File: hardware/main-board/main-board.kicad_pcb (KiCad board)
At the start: 4 copper layers, 105 x 38 mm, 105 parts, among them J1 USB_C_Receptacle_USB2.0, J2 DNI, J3 Display Connector, J4 Conn_01x04, SW1 SW_Push, SW2 SW_Push, SW3 SW_Push, SW4 SW_Push, SW5 SW_Detect, SW6 SW_Boot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

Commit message: Final tweaks for Rev C manufacture
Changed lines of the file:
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@@
 	(title_block
 		(title "Printalyzer UV/VIS Densitometer - Main Board")
-		(date "2024-09-04")
+		(date "2024-09-24")
 		(rev "C")
 		(company "Dektronics, Inc.")
@@
 			(pinfunction "Pin_2")
 			(pintype "passive")
+			(teardrops
+				(best_length_ratio 0.5)
+				(max_length 1)
+				(best_width_ratio 1)
+				(max_width 2)
+				(curve_points 0)
+				(filter_ratio 0.9)
+				(enabled yes)
+				(allow_two_segments yes)
+				(prefer_zone_connections yes)
+			)
 		)
 		(pad "3" smd roundrect
@@
 			(pinfunction "Pin_3")
 			(pintype "passive")
+			(teardrops
+				(best_length_ratio 0.5)
+				(max_length 1)
+				(best_width_ratio 1)
+				(max_width 2)
+				(curve_points 0)
+				(filter_ratio 0.9)
+				(enabled yes)
+				(allow_two_segments yes)
+				(prefer_zone_connections yes)
+			)
 		)
 		(pad "4" smd roundrect
@@
 		(start 61.3 61.066002)
 		(end 61.13 61.236002)
-		(width 0.254)
+		(width 0.2)
 		(layer "F.Cu")
 		(net 1)
@@
 		(start 62.213 55.636)
 		(end 62.336 55.759)
-		(width 0.254)
+		(width 0.2)
 		(layer "F.Cu")
 		(net 1)
@@
 		(start 61.13 61.236002)
 		(end 61.13 61.65)
-		(width 0.254)
+		(width 0.2)
 		(layer "F.Cu")
 		(net 1)
@@
 		(start 62.336 57.537)
 		(end 62.463 57.664)
-		(width 0.254)
+		(width 0.2)
 		(layer "F.Cu")
 		(net 1)
@@
 		(start 61.5 56.636)
 		(end 62.324 56.636)
-		(width 0.254)
+		(width 0.2)
 		(layer "F.Cu")
 		(net 1)
@@
 		(start 61.3 60.2625)
 		(end 61.3 61.066002)
-		(width 0.254)
+		(width 0.2)
 		(layer "F.Cu")
 		(net 1)
@@
 		(start 62.336 56.648)
 		(end 62.336 57.537)
-		(width 0.254)
+		(width 0.2)
 		(layer "F.Cu")
 		(net 1)
@@
 		(start 61.5 55.636)
 		(end 62.213 55.636)
-		(width 0.254)
+		(width 0.2)
 		(layer "F.Cu")
 		(net 1)
@@
 		(start 62.463 57.664)
 		(end 62.971 57.664)
-		(width 0.254)
+		(width 0.2)
 		(layer "F.Cu")
 		(net 1)
@@
 		(start 61.5 56.136)
 		(end 62.332 56.136)
-		(width 0.254)
+		(width 0.2)
 		(layer "F.Cu")
 		(net 1)
@@
 		(start 62.336 56.14)
 		(end 62.336 56.648)
-		(width 0.254)
+		(width 0.2)
 		(layer "F.Cu")
 		(net 1)
@@
 		(start 62.336 55.759)
 		(end 62.336 56.14)
-		(width 0.254)
+		(width 0.2)
 		(layer "F.Cu")
 		(net 1)
@@
 		(start 62.971 56.874)
 		(end 62.971 57.664)
-		(width 0.508)
+		(width 0.381)
 		(layer "F.Cu")
 		(net 1)
@@
 		(start 63.761 55.914)
 		(end 63.86 56.013)
-		(width 0.508)
+		(width 0.381)
 		(layer "F.Cu")
 		(net 2)
@@
 		(start 62.971 55.378)
 		(end 62.971 55.914)
-		(width 0.254)
+		(width 0.2)
 		(layer "F.Cu")
 		(net 2)
@@
 		(start 62.971 55.914)
 		(end 63.761 55.914)
-		(width 0.508)
+		(width 0.381)
 		(layer "F.Cu")
 		(net 2)
@@
 		(start 61.5 55.136)
 		(end 62.729 55.136)
-		(width 0.254)
+		(width 0.2)
 		(layer "F.Cu")
 		(net 2)
@@
 		(start 62.729 55.136)
 		(end 62.971 55.378)
-		(width 0.254)
+		(width 0.2)
 		(layer "F.Cu")
 		(net 2)
@@
 		(start 60 60.2625)
 		(end 60 61.066002)
-		(width 0.254)
+		(width 0.2)
 		(layer "F.Cu")
 		(net 7)
@@
 		(start 60 61.066002)
 		(end 60.17 61.236002)
-		(width 0.254)
+		(width 0.2)
 		(layer "F.Cu")
 		(net 7)
@@
 		(start 60.17 61.236002)
 		(end 60.17 61.65)
-		(width 0.254)
+		(width 0.2)
 		(layer "F.Cu")
 		(net 7)
@@
 		(start 60 59.7375)
 		(end 60 59.4428)
-		(width 0.254)
+		(width 0.2)
 		(layer "F.Cu")
 		(net 23)
@@
 		(start 60 59.4428)
 		(end 59.542 58.9848)
-		(width 0.254)
+		(width 0.2)
 		(layer "F.Cu")
 		(net 23)
@@
 		(start 56.506 55.136)
 		(end 55.986 54.616)
-		(width 0.254)
+		(width 0.2)
 		(layer "F.Cu")
 		(net 23)
@@
 		(start 56.6718 58.9848)
 		(end 56.494 58.807)
-		(width 0.254)
+		(width 0.2)
 		(layer "F.Cu")
 		(net 23)
@@
 		(start 58.6 55.136)
 		(end 56.506 55.136)
-		(width 0.254)
+		(width 0.2)
 		(layer "F.Cu")
 		(net 23)
@@
 		(start 59.542 58.9848)
 		(end 56.6718 58.9848)
-		(width 0.254)
+		(width 0.2)
 		(layer "F.Cu")
 		(net 23)
@@
 		(start 61.3 58.533)
 		(end 61.3 59.7375)
-		(width 0.254)
+		(width 0.2)
 		(layer "F.Cu")
 		(net 24)
@@
 		(start 58.6 55.636)
 		(end 55.863 55.636)
-		(width 0.254)
+		(width 0.2)
 		(layer "F.Cu")
 		(net 24)
@@
 		(start 55.351 58.1466)
 		(end 55.3574 58.153)
-		(width 0.254)
+		(width 0.2)
 		(layer "F.Cu")
 		(net 24)
@@
 		(start 55.3574 58.153)
 		(end 60.92 58.153)
-		(width 0.254)
+		(width 0.2)
 		(layer "F.Cu")
 		(net 24)
@@
 		(start 60.92 58.153)
 		(end 61.3 58.533)
-		(width 0.254)
+		(width 0.2)
 		(layer "F.Cu")
 		(net 24)
@@
 		(start 55.863 55.636)
 		(end 54.843 54.616)
-		(width 0.254)
+		(width 0.2)
 		(layer "F.Cu")
 		(net 24)
@@
 		(start 60.65 59.7375)
 		(end 60.65 59.1)
-		(width 0.254)
+		(width 0.2)
 		(layer "F.Cu")
 		(net 57)
@@
 		(start 60.65 60.2625)
 		(end 60.65 60.9)
-		(width 0.254)
+		(width 0.2)
 		(layer "F.Cu")
 		(net 61)
@@
 		(priority 6)
 		(connect_pads yes
-			(clearance 0.508)
+			(clearance 0.25)
 		)
 		(min_thickness 0.25)
@@
 		(priority 7)
 		(connect_pads yes
-			(clearance 0.508)
+			(clearance 0.25)
 		)
 		(min_thickness 0.25)
@@
 		(priority 6)
 		(connect_pads yes
-			(clearance 0.508)
+			(clearance 0.25)
 		)
 		(min_thickness 0.25)
@@
 		(priority 7)
 		(connect_pads yes
-			(clearance 0.508)
+			(clearance 0.25)
 		)
 		(min_thickness 0.25)
@@
 		(priority 7)
 		(connect_pads yes
-			(clearance 0.508)
+			(clearance 0.25)
 		)
 		(min_thickness 0.25)
@@
 		(priority 6)
 		(connect_pads yes
-			(clearance 0.508)
+			(clearance 0.25)
 		)
 		(min_thickness 0.25)
@@
 		(priority 7)
 		(connect_pads yes
-			(clearance 0.508)
+			(clearance 0.25)
 		)
 		(min_thickness 0.25)
@@
 	)
 	(zone
+		(net 58)
+		(net_name "/TVLED_EN")
+		(layer "F.Cu")
+		(name "$teardrop_padvia$")
+		(hatch full 0.1)
+		(priority 30000)
+		(attr
+			(teardrop
+				(type padvia)
+			)
+		)
+		(connect_pads yes
+			(clearance 0)
+		)
+		(min_thickness 0.0254)
+		(filled_areas_thickness no)
+		(fill yes
+			(thermal_gap 0.5)
+			(thermal_bridge_width 0.5)
+			(island_removal_mode 1)
+			(island_area_min 10)
+		)
+		(polygon
+			(pts
+				(xy 140.599993 70.373012) (xy 140.599993 70.627012) (xy 140.99259 70.788594) (xy 141.675993 70.500012)
+				(xy 140.99259 70.21143)
+			)
+		)
+	)
+	(zone
+		(net 60)
+		(net_name "/TULED_EN")
+		(layer "F.Cu")
+		(name "$teardrop_padvia$")
+		(hatch full 0.1)
+		(priority 30001)
+		(attr
+			(teardrop
+				(type padvia)
+			)
+		)
+		(connect_pads yes
+			(clearance 0)
+		)
+		(min_thickness 0.0254)
+		(filled_areas_thickness no)
+		(fill yes
+			(thermal_gap 0.5)
+			(thermal_bridge_width 0.5)
+			(island_removal_mode 1)
+			(island_area_min 10)
+		)
+		(polygon
+			(pts
+				(xy 140.599993 69.373012) (xy 140.599993 69.627012) (xy 140.99259 69.788594) (xy 141.675993 69.500012)
+				(xy 140.99259 69.21143)
+			)
+		)
+	)
+	(zone
 		(net 21)
 		(net_name "/Sensor Head/RLED3")
@@
 		(priority 6)
 		(connect_pads yes
-			(clearance 0.508)
+			(clearance 0.25)
 		)
 		(min_thickness 0.25)
@@
 		(priority 2)
 		(connect_pads
-			(clearance 0.508)
+			(clearance 0.25)
 		)
 		(min_thickness 0.25)
@@
 		(priority 5)
 		(connect_pads
-			(clearance 0.508)
+			(clearance 0.25)
 		)
 		(min_thickness 0.25)
@@
 		(priority 3)
 		(connect_pads
-			(clearance 0.508)
+			(clearance 0.25)
 		)
 		(min_thickness 0.25)
@@
 		(priority 4)
 		(connect_pads
-			(clearance 0.508)
+			(clearance 0.25)
 		)
 		(min_thickness 0.25)

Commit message: Fix net name for reflection LEDs
This should match the identifer used in the firmware, for consistency
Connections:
- net /RLED_EN renamed /RVLED_EN
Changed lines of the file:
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@@
 	(net 48 "unconnected-(J3-NC-Pad1)")
 	(net 49 "unconnected-(J3-NC-Pad7)")
-	(net 50 "/RLED_EN")
+	(net 50 "/RVLED_EN")
 	(net 51 "unconnected-(J3-D2-Pad20)")
 	(net 52 "+3.3VA")
@@
 		(layer "F.Cu")
 		(at 134.874 59.475 180)
-		(descr "SOT, 6 Pin (https://www.jedec.org/sites/default/files/docs/Mo-178c.PDF variant AB), generated with kicad-footprint-generator ipc_gullwing_generator.py")
+		(descr "SOT, 6 Pin (~), generated with kicad-footprint-generator ipc_gullwing_generator.py")
 		(tags "SOT TO_SOT_SMD")
 		(property "Reference" "U4"
@@
 			(layers "F.Cu" "F.Paste" "F.Mask")
 			(roundrect_rratio 0.25)
-			(net 50 "/RLED_EN")
+			(net 50 "/RVLED_EN")
 			(pinfunction "PB3")
 			(pintype "bidirectional")
@@
 			(layers "F.Cu" "F.Paste" "F.Mask")
 			(roundrect_rratio 0.25)
-			(net 50 "/RLED_EN")
+			(net 50 "/RVLED_EN")
 			(pinfunction "EN")
 			(pintype "input")
@@
 			(layers "F.Cu" "F.Paste" "F.Mask")
 			(roundrect_rratio 0.25)
-			(net 50 "/RLED_EN")
+			(net 50 "/RVLED_EN")
 			(pintype "passive")
 		)
@@
 	)
 	(zone
+		(net 58)
+		(net_name "/TVLED_EN")
+		(layer "F.Cu")
+		(name "$teardrop_padvia$")
+		(hatch full 0.1)
+		(priority 30000)
+		(attr
+			(teardrop
+				(type padvia)
+			)
+		)
+		(connect_pads yes
+			(clearance 0)
+		)
+		(min_thickness 0.0254)
+		(filled_areas_thickness no)
+		(fill yes
+			(thermal_gap 0.5)
+			(thermal_bridge_width 0.5)
+			(island_removal_mode 1)
+			(island_area_min 10)
+		)
+		(polygon
+			(pts
+				(xy 140.599993 70.373012) (xy 140.599993 70.627012) (xy 140.99259 70.788594) (xy 141.675993 70.500012)
+				(xy 140.99259 70.21143)
+			)
+		)
+	)
+	(zone
 		(net 19)
 		(net_name "/Sensor Head/RLED1")
@@
 	)
 	(zone
-		(net 6)
-		(net_name "+5V")
-		(layer "F.Cu")
-		(hatch edge 0.5)
-		(priority 7)
-		(connect_pads yes
-			(clearance 0.25)
-		)
-		(min_thickness 0.25)
-		(filled_areas_thickness no)
-		(fill yes
-			(thermal_gap 0.5)
-			(thermal_bridge_width 0.5)
-		)
-		(polygon
-			(pts
-				(xy 61.5 43.5) (xy 62.25 43.5) (xy 62.5 43.25) (xy 62.5 42) (xy 63.5 42) (xy 63.5 48) (xy 62.5 48)
-				(xy 62.5 46.75) (xy 62.25 46.5) (xy 61.5 46.5)
-			)
-		)
-	)
-	(zone
-		(net 58)
-		(net_name "/TVLED_EN")
+		(net 60)
+		(net_name "/TULED_EN")
 		(layer "F.Cu")
 		(name "$teardrop_padvia$")
 		(hatch full 0.1)
-		(priority 30000)
+		(priority 30001)
 		(attr
 			(teardrop
@@
 		(polygon
 			(pts
-				(xy 140.599993 70.373012) (xy 140.599993 70.627012) (xy 140.99259 70.788594) (xy 141.675993 70.500012)
-				(xy 140.99259 70.21143)
+				(xy 140.599993 69.373012) (xy 140.599993 69.627012) (xy 140.99259 69.788594) (xy 141.675993 69.500012)
+				(xy 140.99259 69.21143)
 			)
 		)
 	)
 	(zone
-		(net 60)
-		(net_name "/TULED_EN")
+		(net 6)
+		(net_name "+5V")
 		(layer "F.Cu")
-		(name "$teardrop_padvia$")
-		(hatch full 0.1)
-		(priority 30001)
-		(attr
-			(teardrop
-				(type padvia)
-			)
-		)
+		(hatch edge 0.5)
+		(priority 7)
 		(connect_pads yes
-			(clearance 0)
+			(clearance 0.25)
 		)
-		(min_thickness 0.0254)
+		(min_thickness 0.25)
 		(filled_areas_thickness no)
 		(fill yes
 			(thermal_gap 0.5)
 			(thermal_bridge_width 0.5)
-			(island_removal_mode 1)
-			(island_area_min 10)
 		)
 		(polygon
 			(pts
-				(xy 140.599993 69.373012) (xy 140.599993 69.627012) (xy 140.99259 69.788594) (xy 141.675993 69.500012)
-				(xy 140.99259 69.21143)
+				(xy 61.5 43.5) (xy 62.25 43.5) (xy 62.5 43.25) (xy 62.5 42) (xy 63.5 42) (xy 63.5 48) (xy 62.5 48)
+				(xy 62.5 46.75) (xy 62.25 46.5) (xy 61.5 46.5)
 			)
 		)

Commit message: Update ESD321 symbols and footprints
Correct the library symbols and footprints used for the ESD321DYAR so
that the reversed pin 1 indiciation of these components still gets
assembled correctly.

Keeping the existing diode footprint with its marking, and adding a
supplemental dot to indicate how pin 1 differs from what this footprint
otherwise suggests.

This should make all the data correct, though an extra note in assembly
guidance will be necessary just in case.

Fix #1
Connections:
- D10 pad 1: Net-(D10-K) -> GND
- D10 pad 2: GND -> Net-(D10-K)
- D11 pad 1: Net-(D11-K) -> GND
- D11 pad 2: GND -> Net-(D11-K)
- D12 pad 1: Net-(D12-K) -> GND
- D12 pad 2: GND -> Net-(D12-K)
- D5 pad 1: Net-(D5-K) -> GND
- D5 pad 2: GND -> Net-(D5-K)
- D6 pad 1: Net-(D6-K) -> GND
- D6 pad 2: GND -> Net-(D6-K)
- D7 pad 1: /RESET -> GND
- D7 pad 2: GND -> /RESET
- D9 pad 1: Net-(D9-K) -> GND
- D9 pad 2: GND -> Net-(D9-K)
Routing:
- net GND: track 103.8 -> 104.4 mm

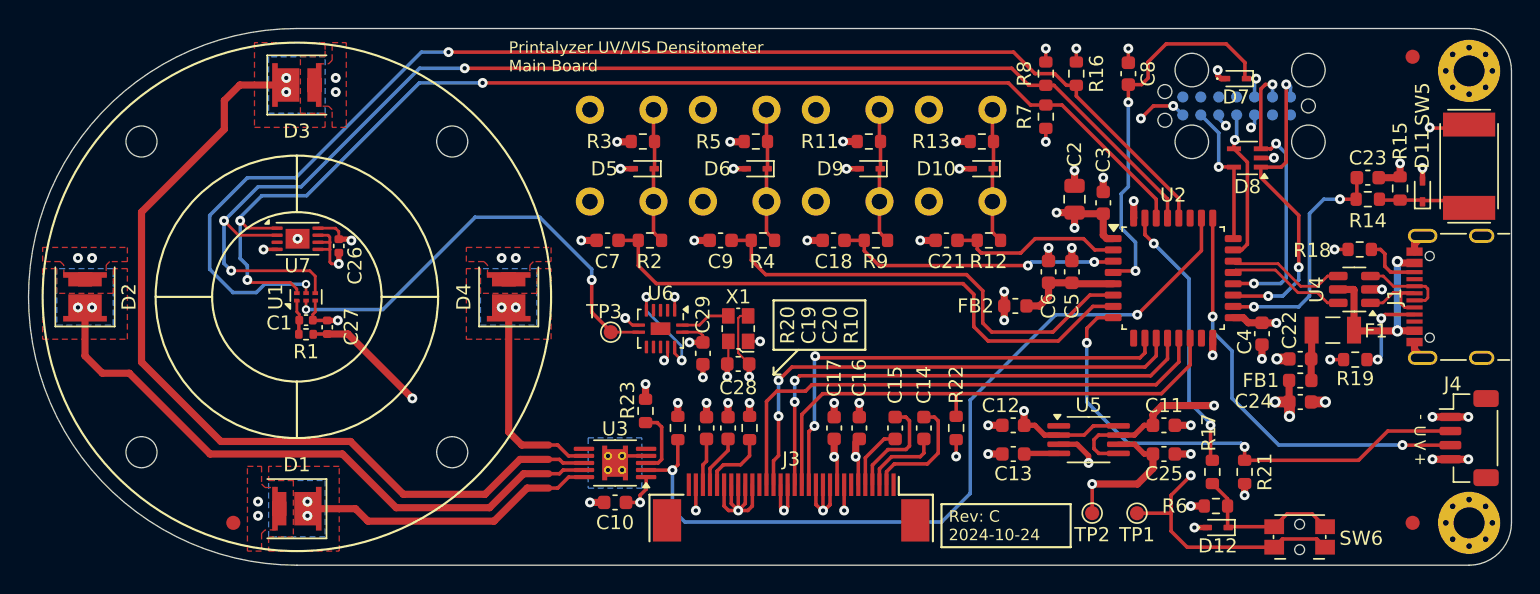
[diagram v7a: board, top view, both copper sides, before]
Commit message: Remove crystal reference and reroute VSYNC pin
In testing with Rev C hardware, it was determined that using the VSYNC
pin to calibrate the TSL2585's internal oscillator can actually
introduce more instability in sensor timing than would otherwise exist.
Furthermore, the most likely factor affecting oscillator stability is
temperature, which we're already planning to correct for.

Thus these extra components should be removed from the design.

For the sake of future-proofing, the VSYNC pin is now rounded directly
to the MCU (though a pull-up resistor), in case someday it is decided to
use this as a measurement trigger. It is also likely this pin will never
be used, but it doesn't really hurt to do this.

Fix #2
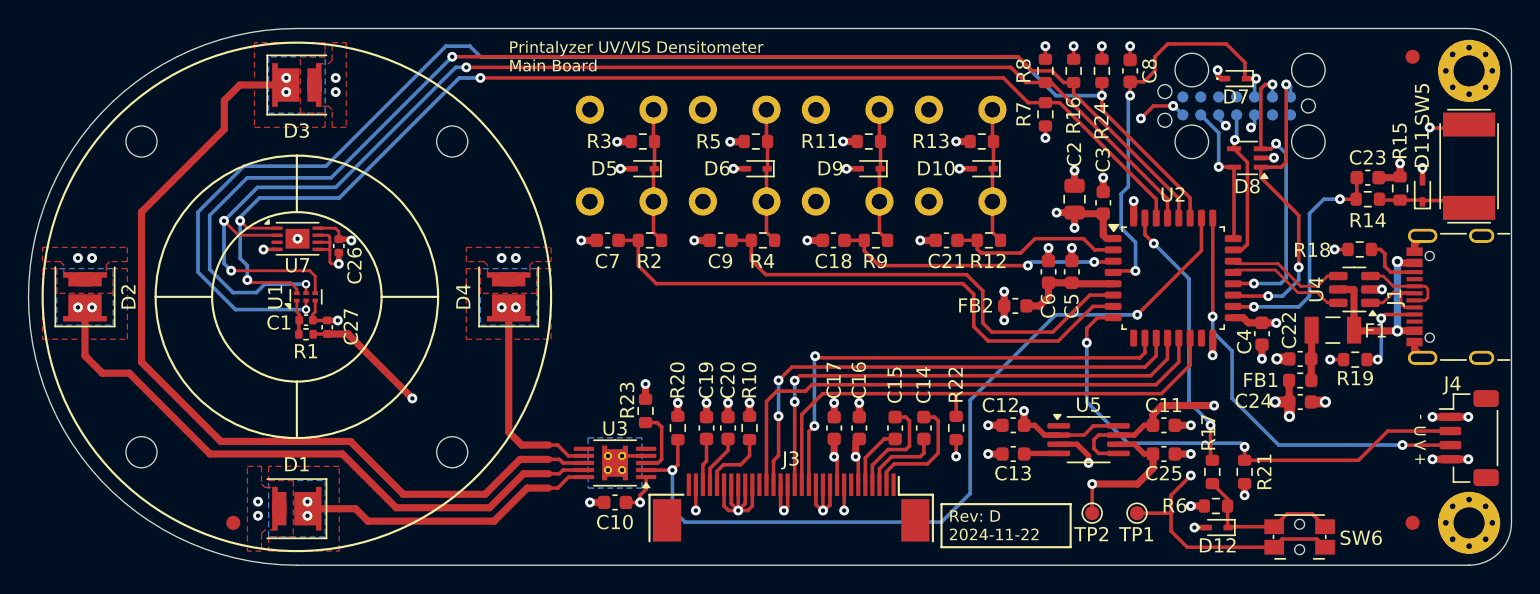
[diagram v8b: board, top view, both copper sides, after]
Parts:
- removed C28, C29: 0.1uF, Capacitor_SMD:C_0603_1608Metric
- removed TP3: 1.8V, TestPoint:TestPoint_Pad_D1.0mm
- removed U6: 74HC393, lib_fp:DHVQFN-14-1EP_2.5x3mm_P0.5mm_EP1x1.5mm
- removed X1: 327MVATX, lib_fp:Oscillator_SMD_ECS_327MVATX-2-4Pin_2.5x2.0mm
- added R24: 10K, Resistor_SMD:R_0603_1608Metric, F.Cu at (117.0, 44.0)
- moved R16 0.27 mm to (115.0, 44.0)
- moved C8 0.23 mm to (119.0, 44.0)
- moved R8 0.20 mm to (113.0, 44.0)
- moved R7 0.17 mm to (113.0, 47.1)
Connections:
- U1 pad 2: /Sensor Head/TSL_VSYNC -> /TSL_VSYNC
- U2 pad 27: unconnected-(U2-PB4-Pad27) -> /TSL_VSYNC
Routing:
- net /TSL_VSYNC: track 0.00 -> 96.1 mm, vias 0 -> 2
- net /Sensor Head/TSL_VSYNC: track 32.1 -> 0.00 mm, vias 2 -> 0
- net GND: track 104.4 -> 95.0 mm, vias 65 -> 60
- net Net-(U6A-Q3): track 7.64 -> 0.00 mm, vias 2 -> 0
- net +3.3V: track 61.4 -> 55.7 mm, vias 18 -> 16
- net Net-(U6A-CP): track 3.52 -> 0.00 mm
